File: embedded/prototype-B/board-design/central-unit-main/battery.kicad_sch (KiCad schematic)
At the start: 15 parts, among them U3 BQ24074RGT

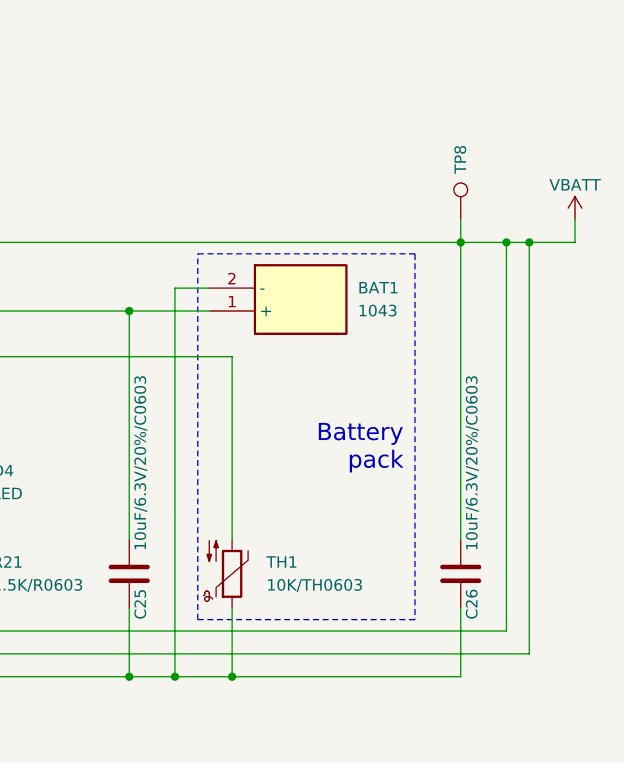
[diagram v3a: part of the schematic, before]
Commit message: [Central Unit] Kicad migration
Migrated the project to the new Kicad version 10.0.3.

Signed-off-by: Nicolae-Andrei Prodan <vasilenicolaeandrei@gmail.com>
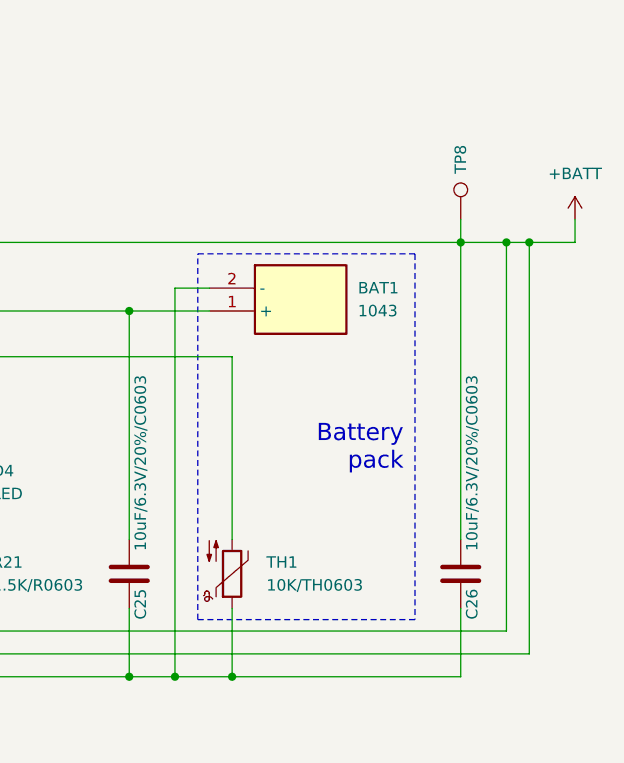
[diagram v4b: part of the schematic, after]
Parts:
- TP8: footprint (none) -> TestPoint:TestPoint_THTPad_D2.0mm_Drill1.0mm
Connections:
- net VBATT renamed +BATT
